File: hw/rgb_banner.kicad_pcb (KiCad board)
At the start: 2 copper layers, 96 x 56 mm, 90 parts, among them P1 +5V, P2 GND, P3 DIN, P4 +5V, P5 GND, P6 DOUT, U1 WS2812B, U10 WS2812B, U11 WS2812B, U12 WS2812B, U13 WS2812B, U14 WS2812B, U15 WS2812B, U16 WS2812B, U17 WS2812B, U18 WS2812B, U19 WS2812B, U2 WS2812B, U20 WS2812B, U21 WS2812B, U22 WS2812B, U23 WS2812B, U24 WS2812B, U25 WS2812B, U26 WS2812B, U27 WS2812B, U28 WS2812B, U29 WS2812B, U3 WS2812B, U30 WS2812B, U31 WS2812B, U32 WS2812B, U33 WS2812B, U34 WS2812B, U35 WS2812B, U36 WS2812B, U37 WS2812B, U38 WS2812B, U39 WS2812B, U4 WS2812B, U40 WS2812B, U41 WS2812B, U42 WS2812B, U43 WS2812B, U44 WS2812B, U45 WS2812B, U46 WS2812B, U47 WS2812B, U48 WS2812B, U49 WS2812B, U5 WS2812B, U50 WS2812B, U51 WS2812B, U52 WS2812B, U53 WS2812B, U54 WS2812B, U55 WS2812B, U56 WS2812B, U57 WS2812B, U58 WS2812B, U59 WS2812B, U6 WS2812B, U60 WS2812B, U61 WS2812B, U62 WS2812B, U63 WS2812B, U64 WS2812B, U65 WS2812B, U66 WS2812B, U67 WS2812B, U68 WS2812B, U69 WS2812B, U7 WS2812B, U70 WS2812B, U71 WS2812B, U72 WS2812B, U73 WS2812B, U74 WS2812B, U75 WS2812B, U76 WS2812B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

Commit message: zones not working
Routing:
- net /+5V: track 8.01 -> 36.3 mm
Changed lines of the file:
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@@
     (thickness 1.6)
     (drawings 4)
-    (tracks 8)
+    (tracks 30)
     (zones 0)
     (modules 90)
@@
     (uvia_dia 0.508)
     (uvia_drill 0.127)
-    (add_net /+5V)
     (add_net /d_in)
     (add_net /d_out)
-    (add_net /gnd)
     (add_net "Net-(U1-Pad2)")
     (add_net "Net-(U10-Pad2)")
@@
     (uvia_dia 0.508)
     (uvia_drill 0.127)
+    (add_net /+5V)
+    (add_net /gnd)
   )
   (module kicadlib:TEST_0.100 (layer F.Cu)
@@
   (gr_line (start 68 108) (end 164 108) (angle 90) (layer Edge.Cuts) (width 0.1))
   (gr_line (start 68 52) (end 68 108) (angle 90) (layer Edge.Cuts) (width 0.1))
-  (segment (start 77.55 62.4) (end 77.55 60.95) (width 0.45) (layer F.Cu) (net 39))
-  (segment (start 77.55 60.95) (end 78 60.5) (width 0.45) (layer F.Cu) (net 39))
-  (segment (start 82.45 57.6) (end 82.45 59.45) (width 0.45) (layer F.Cu) (net 39))
-  (segment (start 82.45 59.45) (end 82.5 59.5) (width 0.45) (layer F.Cu) (net 39))
-  (segment (start 74.45 57.6) (end 74.45 59.45) (width 0.45) (layer F.Cu) (net 39))
-  (segment (start 74.45 59.45) (end 74.5 59.5) (width 0.45) (layer F.Cu) (net 39))
-  (segment (start 69.55 62.4) (end 69.55 60.95) (width 0.45) (layer F.Cu) (net 39))
-  (segment (start 69.55 60.95) (end 70 60.5) (width 0.45) (layer F.Cu) (net 39))
+  (segment (start 125.55 62.4) (end 125.55 60.05) (width 0.45) (layer F.Cu) (net 39))
+  (segment (start 125.55 60.05) (end 125.5 60) (width 0.45) (layer F.Cu) (net 39))
+  (segment (start 122.45 57.6) (end 122.45 59.95) (width 0.45) (layer F.Cu) (net 39))
+  (segment (start 122.45 59.95) (end 122.5 60) (width 0.45) (layer F.Cu) (net 39))
+  (segment (start 117.55 62.4) (end 117.55 60.05) (width 0.45) (layer F.Cu) (net 39))
+  (segment (start 117.55 60.05) (end 117.5 60) (width 0.45) (layer F.Cu) (net 39))
+  (segment (start 114.45 57.6) (end 114.45 59.95) (width 0.45) (layer F.Cu) (net 39))
+  (segment (start 114.45 59.95) (end 114.5 60) (width 0.45) (layer F.Cu) (net 39))
+  (segment (start 109.55 62.4) (end 109.55 60.05) (width 0.45) (layer F.Cu) (net 39))
+  (segment (start 109.55 60.05) (end 109.5 60) (width 0.45) (layer F.Cu) (net 39))
+  (segment (start 106.45 57.6) (end 106.45 59.95) (width 0.45) (layer F.Cu) (net 39))
+  (segment (start 106.45 59.95) (end 106.5 60) (width 0.45) (layer F.Cu) (net 39))
+  (segment (start 101.55 62.4) (end 101.55 60.05) (width 0.45) (layer F.Cu) (net 39))
+  (segment (start 101.55 60.05) (end 101.5 60) (width 0.45) (layer F.Cu) (net 39))
+  (segment (start 98.45 57.6) (end 98.45 59.95) (width 0.45) (layer F.Cu) (net 39))
+  (segment (start 98.45 59.95) (end 98.5 60) (width 0.45) (layer F.Cu) (net 39))
+  (segment (start 93.55 62.4) (end 93.55 60.05) (width 0.45) (layer F.Cu) (net 39))
+  (segment (start 93.55 60.05) (end 93.5 60) (width 0.45) (layer F.Cu) (net 39))
+  (segment (start 85.55 62.4) (end 85.55 60.05) (width 0.45) (layer F.Cu) (net 39))
+  (segment (start 85.55 60.05) (end 85.5 60) (width 0.45) (layer F.Cu) (net 39))
+  (segment (start 90.45 57.6) (end 90.45 59.95) (width 0.45) (layer F.Cu) (net 39))
+  (segment (start 90.45 59.95) (end 90.5 60) (width 0.45) (layer F.Cu) (net 39))
+  (segment (start 82.45 57.6) (end 82.45 59.95) (width 0.45) (layer F.Cu) (net 39))
+  (segment (start 82.45 59.95) (end 82.5 60) (width 0.45) (layer F.Cu) (net 39))
+  (segment (start 77.55 62.4) (end 77.55 60.05) (width 0.45) (layer F.Cu) (net 39))
+  (segment (start 77.55 60.05) (end 77.5 60) (width 0.45) (layer F.Cu) (net 39))
+  (segment (start 69.55 62.4) (end 69.55 60.05) (width 0.45) (layer F.Cu) (net 39))
+  (segment (start 69.55 60.05) (end 69.5 60) (width 0.45) (layer F.Cu) (net 39))
+  (segment (start 74.45 57.6) (end 74.45 59.95) (width 0.45) (layer F.Cu) (net 39))
+  (segment (start 74.45 59.95) (end 74.5 60) (width 0.45) (layer F.Cu) (net 39))
   (zone (net 4) (net_name /digit1/+5V) (layer F.Cu) (hatch edge 0.508)
     (connect_pads (clearance 0.254))

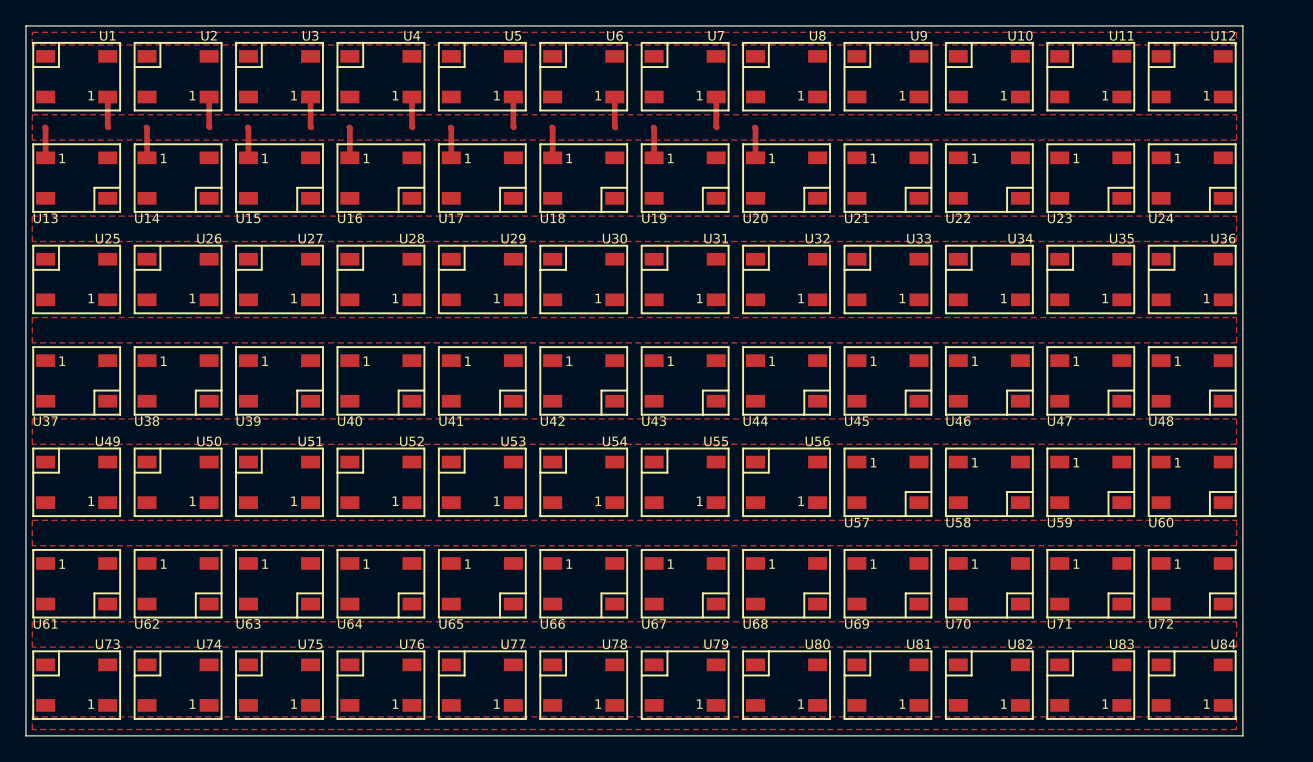
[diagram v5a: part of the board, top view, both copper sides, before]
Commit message: zone fill by setting to no_net, filling, then setting correct net.
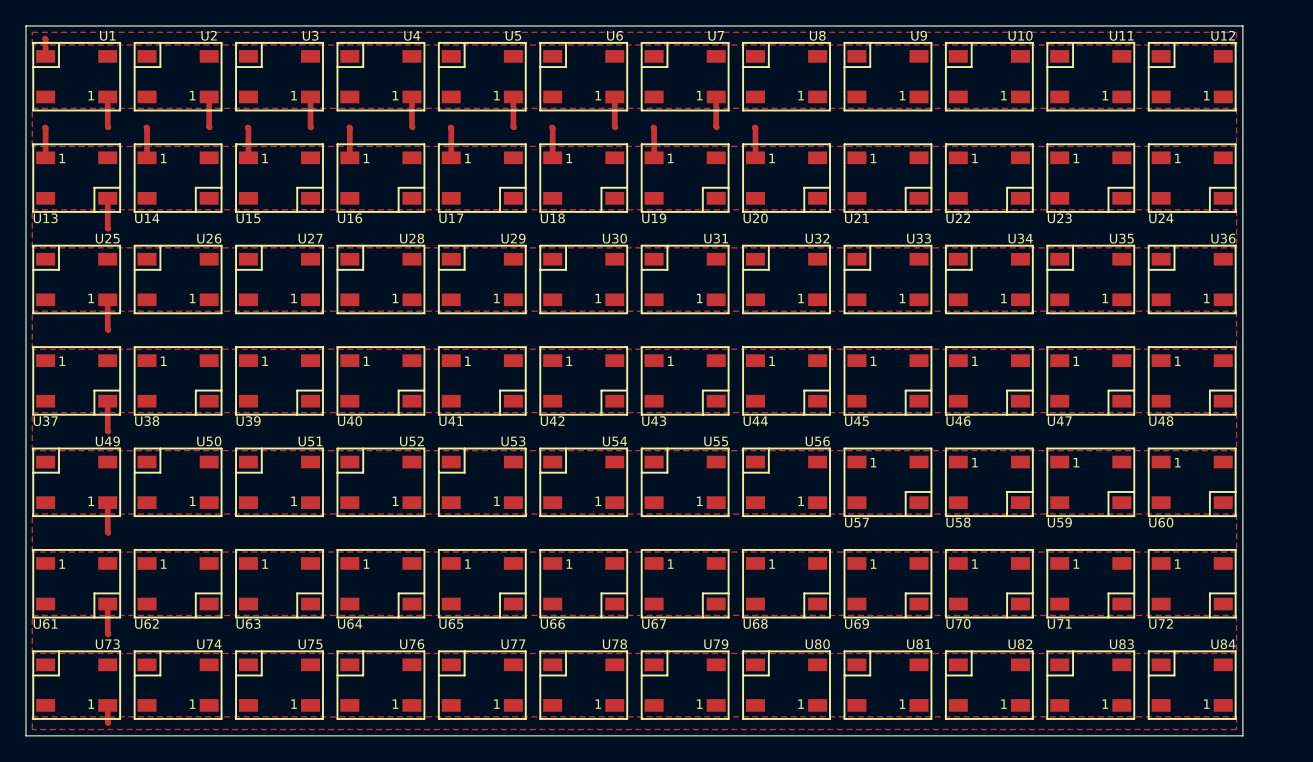
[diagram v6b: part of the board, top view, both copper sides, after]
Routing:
- net /gnd: track 0.00 -> 8.68 mm
- net /+5V: track 36.3 -> 42.6 mm
- removed copper zone on F.Cu, net /digit1/+5V
